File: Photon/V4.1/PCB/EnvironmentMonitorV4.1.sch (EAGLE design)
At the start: 29 parts, among them U5 CCS811, U6 BME280, U7 ALS-PT19, U8 ALS-PT19

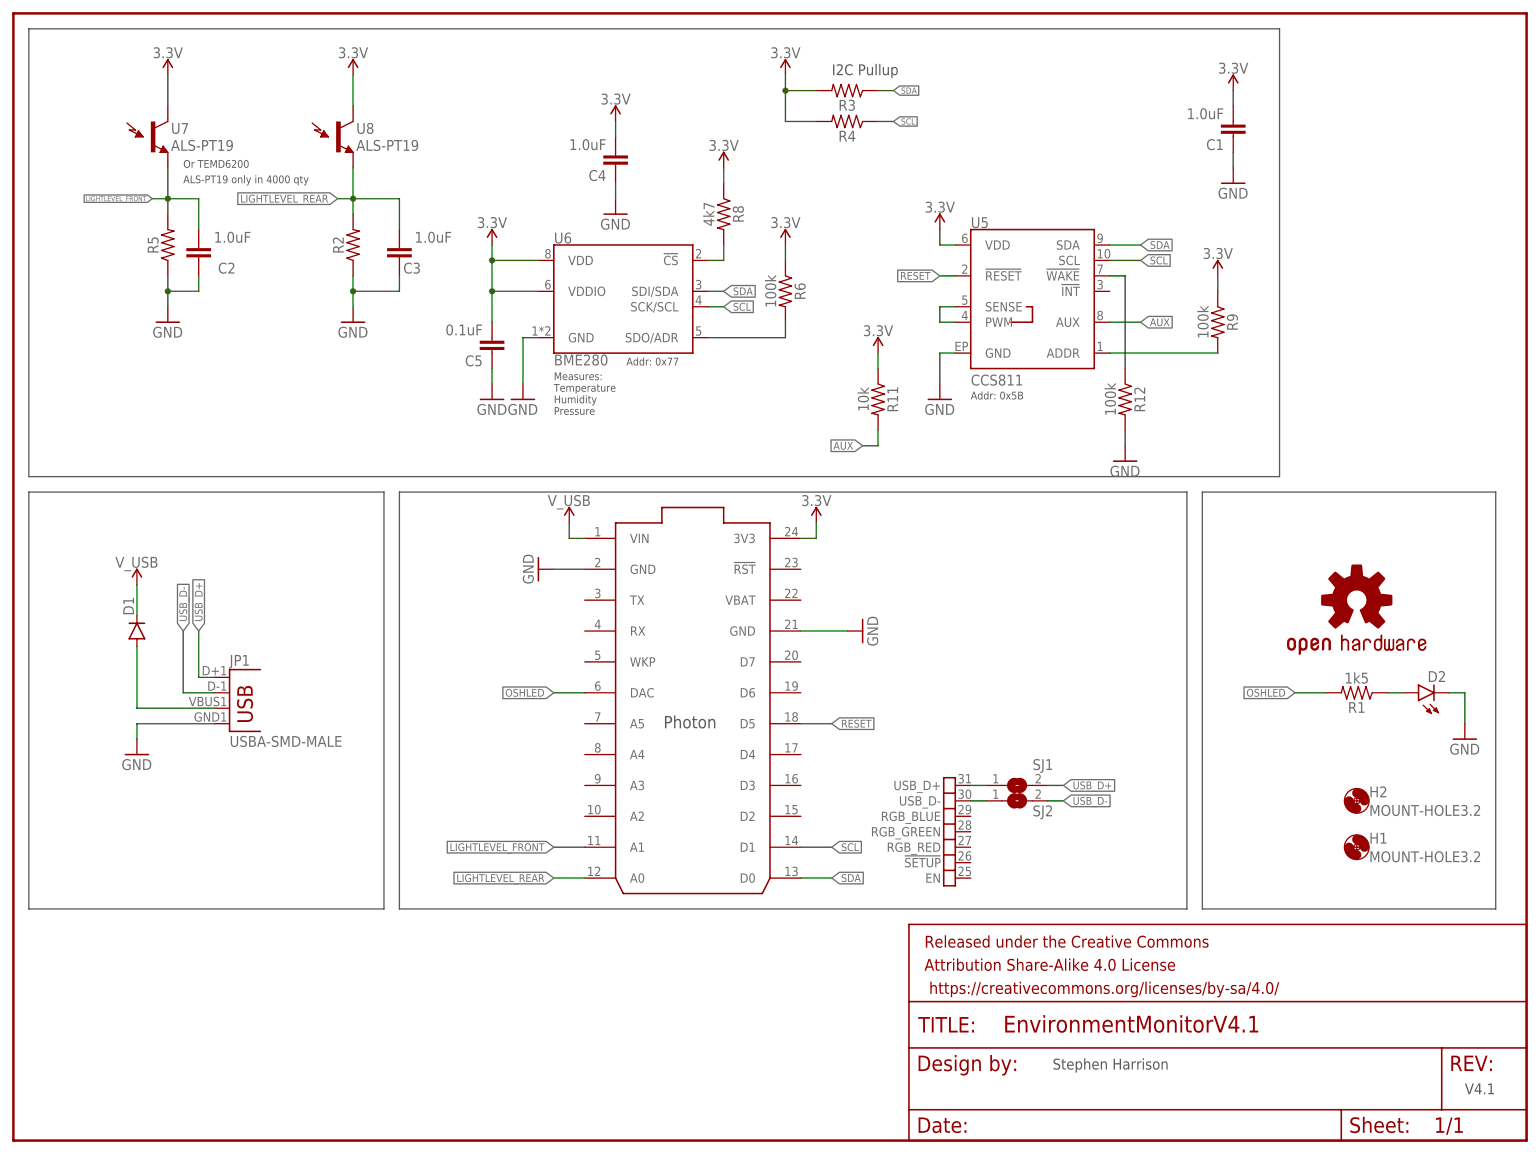
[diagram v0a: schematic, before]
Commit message: Updated library and set part values.
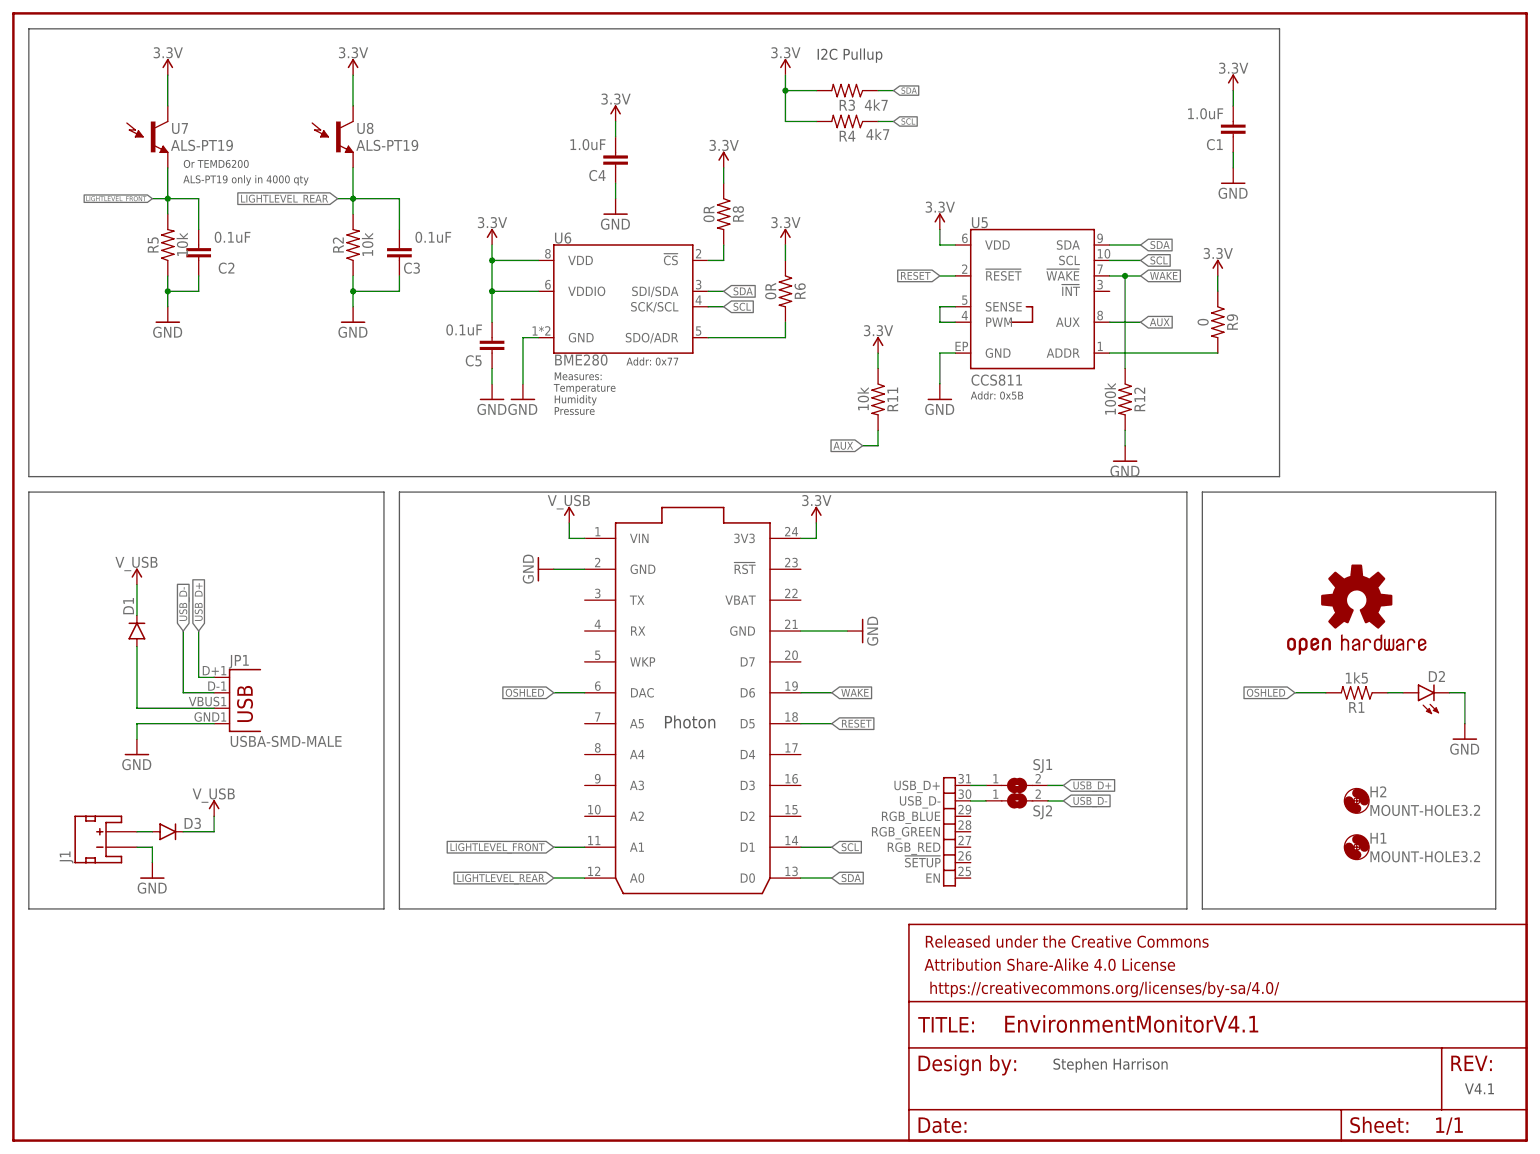
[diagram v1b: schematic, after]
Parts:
- added D3: (no value), SparkFun-DiscreteSemi:DIODESMA
- added J1: (no value), SparkFun-Connectors:JST_2MM_MALE
- C2, C3: value 1.0uF -> 0.1uF
- R2, R5: value (none) -> 10k
- R3, R4: value (none) -> 4k7
- R6: value 100k -> 0R
- R8: value 4k7 -> 0R
- R9: value 100k -> 0
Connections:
- new net N$4: D3.A, J1.+
- net GND: now also J1.-
- net V_USB: now also D3.C
- net WAKE: now also U$1G$1.D6
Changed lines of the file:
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@@
 <part name="JP1" library="Tinamous" deviceset="USB" device="A-SMD-MALE"/>
 <part name="GND1" library="SparkFun-Aesthetics" deviceset="GND" device=""/>
-<part name="R3" library="SparkFun-Resistors" deviceset="RESISTOR" device="0805" value=" "/>
-<part name="R4" library="SparkFun-Resistors" deviceset="RESISTOR" device="0805" value=" "/>
+<part name="R3" library="SparkFun-Resistors" deviceset="RESISTOR" device="0805" value="4k7"/>
+<part name="R4" library="SparkFun-Resistors" deviceset="RESISTOR" device="0805" value="4k7"/>
 <part name="C4" library="SparkFun-Capacitors" deviceset="1.0UF-25V-+80/-20(0805)" device="&quot;" value="1.0uF"/>
 <part name="H1" library="holes" deviceset="MOUNT-HOLE" device="3.2" value="MOUNT-HOLE3.2"/>
@@
 <part name="U7" library="SparkFun-Sensors" deviceset="LIGHT_SENSOR" device="ALS" value="ALS-PT19"/>
 <part name="U8" library="SparkFun-Sensors" deviceset="LIGHT_SENSOR" device="ALS" value="ALS-PT19"/>
-<part name="R2" library="SparkFun-Resistors" deviceset="RESISTOR" device="0805" value=" "/>
-<part name="R5" library="SparkFun-Resistors" deviceset="RESISTOR" device="0805" value=" "/>
-<part name="C2" library="SparkFun-Capacitors" deviceset="1.0UF-25V-+80/-20(0805)" device="&quot;" value="1.0uF"/>
-<part name="C3" library="SparkFun-Capacitors" deviceset="1.0UF-25V-+80/-20(0805)" device="&quot;" value="1.0uF"/>
+<part name="R2" library="SparkFun-Resistors" deviceset="RESISTOR" device="0805" value="10k"/>
+<part name="R5" library="SparkFun-Resistors" deviceset="RESISTOR" device="0805" value="10k"/>
+<part name="C2" library="SparkFun-Capacitors" deviceset="1.0UF-25V-+80/-20(0805)" device="&quot;" value="0.1uF"/>
+<part name="C3" library="SparkFun-Capacitors" deviceset="1.0UF-25V-+80/-20(0805)" device="&quot;" value="0.1uF"/>
 <part name="SUPPLY4" library="SparkFun-PowerSymbols" deviceset="3.3V" device=""/>
 <part name="GND4" library="SparkFun-Aesthetics" deviceset="GND" device=""/>
 <part name="SUPPLY6" library="SparkFun-PowerSymbols" deviceset="3.3V" device=""/>
-<part name="R6" library="SparkFun-Resistors" deviceset="RESISTOR" device="0805" value="100k"/>
+<part name="R6" library="SparkFun-Resistors" deviceset="RESISTOR" device="0805" value="0R"/>
 <part name="GND9" library="SparkFun-Aesthetics" deviceset="GND" device=""/>
 <part name="SUPPLY9" library="SparkFun-PowerSymbols" deviceset="3.3V" device=""/>
@@
 <part name="SUPPLY12" library="SparkFun-PowerSymbols" deviceset="3.3V" device=""/>
 <part name="GND12" library="SparkFun-Aesthetics" deviceset="GND" device=""/>
-<part name="R8" library="SparkFun-Resistors" deviceset="RESISTOR" device="0805" value="4k7"/>
+<part name="R8" library="SparkFun-Resistors" deviceset="RESISTOR" device="0805" value="0R"/>
 <part name="SUPPLY14" library="SparkFun-PowerSymbols" deviceset="3.3V" device=""/>
 <part name="GND15" library="SparkFun-Aesthetics" deviceset="GND" device=""/>
 <part name="SUPPLY15" library="SparkFun-PowerSymbols" deviceset="3.3V" device=""/>
-<part name="R9" library="SparkFun-Resistors" deviceset="RESISTOR" device="0805" value="100k"/>
+<part name="R9" library="SparkFun-Resistors" deviceset="RESISTOR" device="0805" value="0"/>
 <part name="R11" library="SparkFun-Resistors" deviceset="RESISTOR" device="0805" value="10k"/>
 <part name="SUPPLY16" library="SparkFun-PowerSymbols" deviceset="3.3V" device=""/>
@@
 <part name="SJ1" library="jumper" deviceset="SJ" device=""/>
 <part name="SJ2" library="jumper" deviceset="SJ" device=""/>
+<part name="J1" library="SparkFun-Connectors" deviceset="JST_2MM_MALE" device=""/>
+<part name="D3" library="SparkFun-DiscreteSemi" deviceset="DIODE" device="SMA"/>
+<part name="GND2" library="SparkFun-Aesthetics" deviceset="GND" device=""/>
+<part name="SUPPLY1" library="SparkFun-PowerSymbols" deviceset="V_USB" device=""/>
 </parts>
 <sheets>
 <sheet>
 <plain>
-<text x="134.62" y="175.26" size="1.778" layer="97">I2C Pullup</text>
+<text x="132.08" y="177.8" size="1.778" layer="97">I2C Pullup</text>
 <wire x1="2.54" y1="182.88" x2="2.54" y2="109.22" width="0.1524" layer="97"/>
 <wire x1="2.54" y1="109.22" x2="208.28" y2="109.22" width="0.1524" layer="97"/>
@@
 <instance part="JP1" gate="G$1" x="35.56" y="68.58"/>
 <instance part="GND1" gate="1" x="20.32" y="63.5"/>
-<instance part="R3" gate="G$1" x="137.16" y="172.72" rot="R180"/>
-<instance part="R4" gate="G$1" x="137.16" y="167.64" rot="R180"/>
+<instance part="R3" gate="G$1" x="137.16" y="172.72" smashed="yes" rot="R180">
+<attribute name="NAME" x="137.16" y="171.196" size="1.778" layer="95" font="vector" rot="R180" align="bottom-center"/>
+<attribute name="VALUE" x="141.986" y="169.418" size="1.778" layer="96" font="vector" rot="R180" align="top-center"/>
+</instance>
+<instance part="R4" gate="G$1" x="137.16" y="167.64" smashed="yes" rot="R180">
+<attribute name="NAME" x="137.16" y="166.116" size="1.778" layer="95" font="vector" rot="R180" align="bottom-center"/>
+<attribute name="VALUE" x="142.24" y="164.592" size="1.778" layer="96" font="vector" rot="R180" align="top-center"/>
+</instance>
 <instance part="C4" gate="G$1" x="99.06" y="162.56" rot="R180"/>
 <instance part="H1" gate="G$1" x="220.98" y="48.26"/>
@@
 <attribute name="VALUE" x="162.56" y="52.07" size="1.778" layer="96"/>
 </instance>
+<instance part="J1" gate="G$1" x="15.24" y="48.26" rot="R90"/>
+<instance part="D3" gate="G$1" x="25.4" y="50.8"/>
+<instance part="GND2" gate="1" x="22.86" y="43.18"/>
+<instance part="SUPPLY1" gate="G$1" x="33.02" y="53.34"/>
 </instances>
 <busses>
@@
 <pinref part="U$1" gate="G$1" pin="GND@2"/>
 <wire x1="88.9" y1="93.98" x2="93.98" y2="93.98" width="0.1524" layer="91"/>
+</segment>
+<segment>
+<pinref part="J1" gate="G$1" pin="-"/>
+<wire x1="20.32" y1="48.26" x2="22.86" y2="48.26" width="0.1524" layer="91"/>
+<wire x1="22.86" y1="48.26" x2="22.86" y2="45.72" width="0.1524" layer="91"/>
+<pinref part="GND2" gate="1" pin="GND"/>
 </segment>
 </net>
@@
 <wire x1="91.44" y1="99.06" x2="91.44" y2="101.6" width="0.1524" layer="91"/>
 </segment>
+<segment>
+<pinref part="D3" gate="G$1" pin="C"/>
+<wire x1="27.94" y1="50.8" x2="33.02" y2="50.8" width="0.1524" layer="91"/>
+<wire x1="33.02" y1="50.8" x2="33.02" y2="53.34" width="0.1524" layer="91"/>
+<pinref part="SUPPLY1" gate="G$1" pin="V_USB"/>
+</segment>
 </net>
 <net name="LIGHTLEVEL_REAR" class="0">
@@
 <pinref part="R12" gate="G$1" pin="1"/>
 <wire x1="182.88" y1="127" x2="182.88" y2="142.24" width="0.1524" layer="91"/>
+<wire x1="182.88" y1="142.24" x2="185.42" y2="142.24" width="0.1524" layer="91"/>
+<label x="185.42" y="142.24" size="1.27" layer="95" xref="yes"/>
+<junction x="182.88" y="142.24"/>
+</segment>
+<segment>
+<pinref part="U$1" gate="G$1" pin="D6"/>
+<wire x1="129.54" y1="73.66" x2="134.62" y2="73.66" width="0.1524" layer="91"/>
+<label x="134.62" y="73.66" size="1.27" layer="95" xref="yes"/>
 </segment>
 </net>
@@
 </segment>
 </net>
+<net name="N$4" class="0">
+<segment>
+<pinref part="J1" gate="G$1" pin="+"/>
+<pinref part="D3" gate="G$1" pin="A"/>
+<wire x1="20.32" y1="50.8" x2="22.86" y2="50.8" width="0.1524" layer="91"/>
+</segment>
+</net>
